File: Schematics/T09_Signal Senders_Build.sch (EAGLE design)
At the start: 35 parts, among them IC1 7805TV, IC2 7805TV, IC3 ATMEGA328, SW1 , X1 , Y2 16MHz

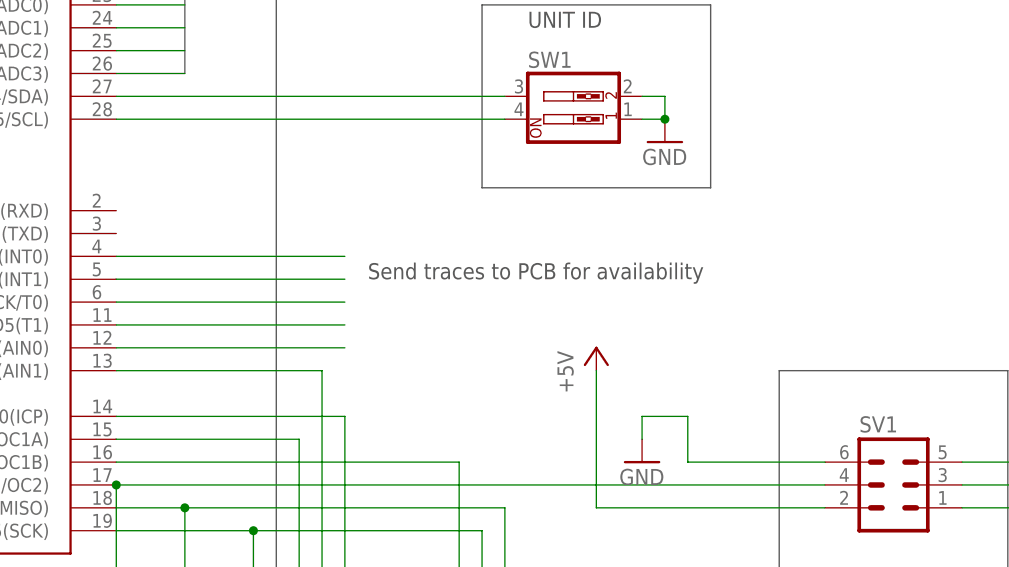
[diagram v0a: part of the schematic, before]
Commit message: PCB - added vias, added headers to uC unused pins
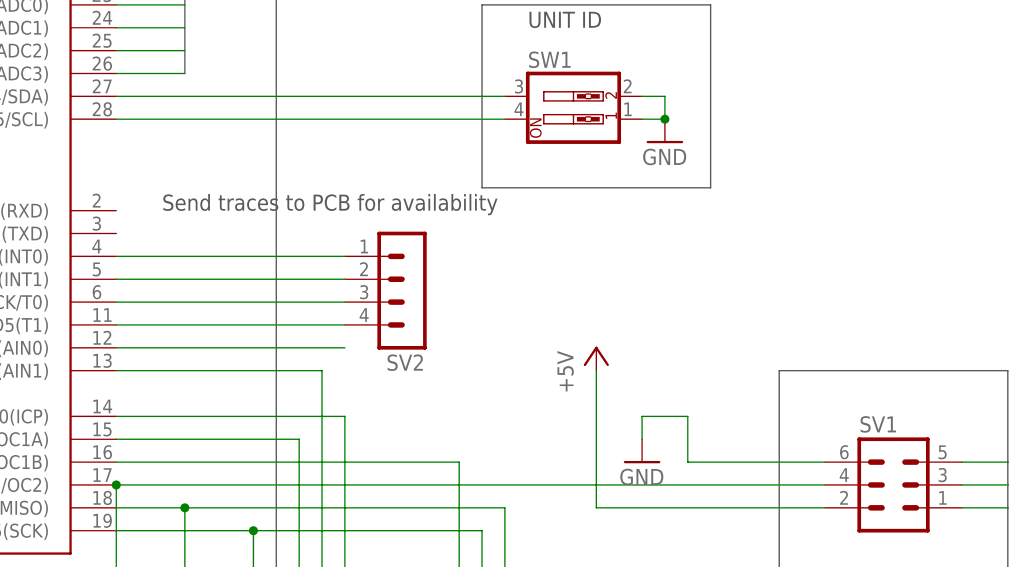
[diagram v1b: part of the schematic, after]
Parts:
- added SV2: (no value), con-lstb:MA04-1
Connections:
- net N$11: now also SV2.1
- net N$12: now also SV2.2
- net N$15: now also SV2.3
- net N$16: now also SV2.4
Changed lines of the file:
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@@
 <layer number="91" name="Nets" color="2" fill="1" visible="yes" active="yes"/>
 <layer number="92" name="Busses" color="1" fill="1" visible="yes" active="yes"/>
-<layer number="93" name="Pins" color="2" fill="1" visible="no" active="yes"/>
+<layer number="93" name="Pins" color="2" fill="1" visible="yes" active="yes"/>
 <layer number="94" name="Symbols" color="4" fill="1" visible="yes" active="yes"/>
 <layer number="95" name="Names" color="7" fill="1" visible="yes" active="yes"/>
 <layer number="96" name="Values" color="7" fill="1" visible="yes" active="yes"/>
 <layer number="97" name="Info" color="7" fill="1" visible="yes" active="yes"/>
-<layer number="98" name="Guide" color="6" fill="1" visible="no" active="yes"/>
+<layer number="98" name="Guide" color="6" fill="1" visible="yes" active="yes"/>
 <layer number="100" name="Muster" color="7" fill="1" visible="no" active="no"/>
-<layer number="101" name="Patch_Top" color="12" fill="4" visible="no" active="yes"/>
-<layer number="102" name="Vscore" color="7" fill="1" visible="no" active="yes"/>
-<layer number="103" name="tMap" color="7" fill="1" visible="no" active="yes"/>
-<layer number="104" name="Name" color="16" fill="1" visible="no" active="yes"/>
-<layer number="105" name="tPlate" color="7" fill="1" visible="no" active="yes"/>
-<layer number="106" name="bPlate" color="7" fill="1" visible="no" active="yes"/>
-<layer number="107" name="Crop" color="7" fill="1" visible="no" active="yes"/>
+<layer number="101" name="Patch_Top" color="12" fill="4" visible="yes" active="yes"/>
+<layer number="102" name="Vscore" color="7" fill="1" visible="yes" active="yes"/>
+<layer number="103" name="tMap" color="7" fill="1" visible="yes" active="yes"/>
+<layer number="104" name="Name" color="16" fill="1" visible="yes" active="yes"/>
+<layer number="105" name="tPlate" color="7" fill="1" visible="yes" active="yes"/>
+<layer number="106" name="bPlate" color="7" fill="1" visible="yes" active="yes"/>
+<layer number="107" name="Crop" color="7" fill="1" visible="yes" active="yes"/>
 <layer number="108" name="tplace-old" color="10" fill="1" visible="yes" active="yes"/>
 <layer number="109" name="ref-old" color="11" fill="1" visible="yes" active="yes"/>
-<layer number="116" name="Patch_BOT" color="9" fill="4" visible="no" active="yes"/>
-<layer number="121" name="_tsilk" color="7" fill="1" visible="no" active="yes"/>
-<layer number="122" name="_bsilk" color="7" fill="1" visible="no" active="yes"/>
-<layer number="125" name="_tNames" color="7" fill="1" visible="no" active="yes"/>
-<layer number="144" name="Drill_legend" color="7" fill="1" visible="no" active="yes"/>
-<layer number="151" name="HeatSink" color="7" fill="1" visible="no" active="yes"/>
+<layer number="116" name="Patch_BOT" color="9" fill="4" visible="yes" active="yes"/>
+<layer number="121" name="_tsilk" color="7" fill="1" visible="yes" active="yes"/>
+<layer number="122" name="_bsilk" color="7" fill="1" visible="yes" active="yes"/>
+<layer number="125" name="_tNames" color="7" fill="1" visible="yes" active="yes"/>
+<layer number="144" name="Drill_legend" color="7" fill="1" visible="yes" active="yes"/>
+<layer number="151" name="HeatSink" color="7" fill="1" visible="yes" active="yes"/>
 <layer number="199" name="Contour" color="7" fill="1" visible="yes" active="yes"/>
-<layer number="200" name="200bmp" color="1" fill="10" visible="no" active="yes"/>
-<layer number="201" name="201bmp" color="2" fill="10" visible="no" active="yes"/>
-<layer number="202" name="202bmp" color="3" fill="10" visible="no" active="yes"/>
-<layer number="203" name="203bmp" color="4" fill="10" visible="no" active="yes"/>
-<layer number="204" name="204bmp" color="5" fill="10" visible="no" active="yes"/>
-<layer number="205" name="205bmp" color="6" fill="10" visible="no" active="yes"/>
-<layer number="206" name="206bmp" color="7" fill="10" visible="no" active="yes"/>
-<layer number="207" name="207bmp" color="8" fill="10" visible="no" active="yes"/>
-<layer number="208" name="208bmp" color="9" fill="10" visible="no" active="yes"/>
-<layer number="209" name="209bmp" color="7" fill="1" visible="no" active="yes"/>
-<layer number="210" name="210bmp" color="7" fill="1" visible="no" active="yes"/>
-<layer number="211" name="211bmp" color="7" fill="1" visible="no" active="yes"/>
-<layer number="212" name="212bmp" color="7" fill="1" visible="no" active="yes"/>
-<layer number="213" name="213bmp" color="7" fill="1" visible="no" active="yes"/>
-<layer number="214" name="214bmp" color="7" fill="1" visible="no" active="yes"/>
-<layer number="215" name="215bmp" color="7" fill="1" visible="no" active="yes"/>
-<layer number="216" name="216bmp" color="7" fill="1" visible="no" active="yes"/>
+<layer number="200" name="200bmp" color="1" fill="10" visible="yes" active="yes"/>
+<layer number="201" name="201bmp" color="2" fill="10" visible="yes" active="yes"/>
+<layer number="202" name="202bmp" color="3" fill="10" visible="yes" active="yes"/>
+<layer number="203" name="203bmp" color="4" fill="10" visible="yes" active="yes"/>
+<layer number="204" name="204bmp" color="5" fill="10" visible="yes" active="yes"/>
+<layer number="205" name="205bmp" color="6" fill="10" visible="yes" active="yes"/>
+<layer number="206" name="206bmp" color="7" fill="10" visible="yes" active="yes"/>
+<layer number="207" name="207bmp" color="8" fill="10" visible="yes" active="yes"/>
+<layer number="208" name="208bmp" color="9" fill="10" visible="yes" active="yes"/>
+<layer number="209" name="209bmp" color="7" fill="1" visible="yes" active="yes"/>
+<layer number="210" name="210bmp" color="7" fill="1" visible="yes" active="yes"/>
+<layer number="211" name="211bmp" color="7" fill="1" visible="yes" active="yes"/>
+<layer number="212" name="212bmp" color="7" fill="1" visible="yes" active="yes"/>
+<layer number="213" name="213bmp" color="7" fill="1" visible="yes" active="yes"/>
+<layer number="214" name="214bmp" color="7" fill="1" visible="yes" active="yes"/>
+<layer number="215" name="215bmp" color="7" fill="1" visible="yes" active="yes"/>
+<layer number="216" name="216bmp" color="7" fill="1" visible="yes" active="yes"/>
 <layer number="217" name="217bmp" color="18" fill="1" visible="no" active="no"/>
 <layer number="218" name="218bmp" color="19" fill="1" visible="no" active="no"/>
@@
 <layer number="250" name="Descript" color="3" fill="1" visible="no" active="no"/>
 <layer number="251" name="SMDround" color="12" fill="11" visible="no" active="no"/>
-<layer number="254" name="cooling" color="7" fill="1" visible="no" active="yes"/>
+<layer number="254" name="cooling" color="7" fill="1" visible="yes" active="yes"/>
 </layers>
 <schematic xreflabel="%F%N/%S.%C%R" xrefpart="/%S.%C%R">
@@
 <part name="P+7" library="supply1" deviceset="+5V" device=""/>
 <part name="GND16" library="supply1" deviceset="GND" device=""/>
+<part name="SV2" library="con-lstb" deviceset="MA04-1" device=""/>
 </parts>
 <sheets>
@@
 <wire x1="147.32" y1="81.28" x2="147.32" y2="182.88" width="0.1524" layer="97"/>
 <wire x1="147.32" y1="182.88" x2="254" y2="182.88" width="0.1524" layer="97"/>
-<text x="264.16" y="119.38" size="1.778" layer="97">Send traces to PCB for availability</text>
+<text x="241.3" y="127" size="1.778" layer="97">Send traces to PCB for availability</text>
 <wire x1="177.8" y1="248.92" x2="177.8" y2="200.66" width="0.1524" layer="97"/>
 <text x="10.16" y="254" size="1.778" layer="97">Connects to a DC barrel on the wall of the unit.
@@
 <instance part="P+7" gate="1" x="289.56" y="111.76"/>
 <instance part="GND16" gate="1" x="294.64" y="99.06"/>
+<instance part="SV2" gate="1" x="269.24" y="116.84" rot="R180"/>
 </instances>
 <busses>
@@
 <pinref part="IC3" gate="G$1" pin="PD2(INT0)"/>
 <wire x1="236.22" y1="121.92" x2="261.62" y2="121.92" width="0.1524" layer="91"/>
+<pinref part="SV2" gate="1" pin="1"/>
 </segment>
 </net>
@@
 <pinref part="IC3" gate="G$1" pin="PD3(INT1)"/>
 <wire x1="236.22" y1="119.38" x2="261.62" y2="119.38" width="0.1524" layer="91"/>
+<pinref part="SV2" gate="1" pin="2"/>
 </segment>
 </net>
@@
 <pinref part="IC3" gate="G$1" pin="PD4(XCK/T0)"/>
 <wire x1="236.22" y1="116.84" x2="261.62" y2="116.84" width="0.1524" layer="91"/>
+<pinref part="SV2" gate="1" pin="3"/>
 </segment>
 </net>
@@
 <pinref part="IC3" gate="G$1" pin="PD5(T1)"/>
 <wire x1="236.22" y1="114.3" x2="261.62" y2="114.3" width="0.1524" layer="91"/>
-</segment>
-</net>
+<pinref part="SV2" gate="1" pin="4"/>
+</segment>
+</net>

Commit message: Fixed Nets. Fixed Silkscreen Layer
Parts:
- 5: value RED -> POWER
- JP1: value (none) -> RF
- JP2: value (none) -> IR
- JP3: value (none) -> Battery; device pinhead:PINHD-1X2/90 -> pinhead:PINHD-1X2
- JP4, JP5, JP6: device pinhead:PINHD-1X2/90 -> pinhead:PINHD-1X2
- LED1: value RED -> WEST
- LED2: value GREEN -> EAST
- LED3: value YELLOW -> SOUTH
- LED4: value BLUE -> NORTH
- S2: value TL32YO -> POWER
- SV1: value (none) -> SPI
- SW1: value (none) -> UNIT_ID
- renumbered LED5 to 5
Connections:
- net RF_SPDSCSC renamed N$35
- net RF_SPI5 renamed N$33
- net RF_SPIDSCSD renamed N$39
- removed net RF_SPIDSCS: IC3.PB4(MISO), JP1.7, JP5.1, JP5.2, SV1.1
- removed net RF_SPIDSCSC: IC3.PB3(MOSI/OC2), JP1.6, JP6.1, JP6.2, SV1.4
- removed net SPI_CE: IC3.PB0(ICP), IC3.PB2(SS/OC1B), JP1.3, JP1.4
- new net N$31: IC3.PB3(MOSI/OC2), IC3.PB4(MISO), JP5.1, JP6.1, SV1.1, SV1.4
- new net N$34: IC3.PB0(ICP), JP1.4
- new net N$36: IC3.PB2(SS/OC1B), JP1.3
- new net N$37: JP1.6, JP6.2
- new net N$38: JP1.7, JP5.2
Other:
- moved on the sheet: C3, JP2, SV1

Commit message: RF nets still had errors. Still need to be routed.
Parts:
- SV2: value (none) -> (none)
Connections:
- new net N$32: IC3.PB3(MOSI/OC2), JP6.1, SV1.4
- net N$31: no longer IC3.PB3(MOSI/OC2), JP6.1, SV1.4
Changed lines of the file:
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@@
 <part name="P+7" library="supply1" deviceset="+5V" device=""/>
 <part name="GND16" library="supply1" deviceset="GND" device=""/>
-<part name="SV2" library="con-lstb" deviceset="MA04-1" device=""/>
+<part name="SV2" library="con-lstb" deviceset="MA04-1" device="" value=" "/>
 </parts>
 <sheets>
@@
 </segment>
 </net>
-<net name="N$31" class="0">
-<segment>
-<pinref part="IC3" gate="G$1" pin="PB3(MOSI/OC2)"/>
-<wire x1="236.22" y1="96.52" x2="304.8" y2="96.52" width="0.1524" layer="91"/>
-<wire x1="304.8" y1="96.52" x2="304.8" y2="104.14" width="0.1524" layer="91"/>
-<pinref part="SV1" gate="1" pin="4"/>
-<wire x1="304.8" y1="104.14" x2="314.96" y2="104.14" width="0.1524" layer="91"/>
-<pinref part="JP6" gate="G$1" pin="1"/>
-<wire x1="236.22" y1="96.52" x2="236.22" y2="93.98" width="0.1524" layer="91"/>
-<pinref part="IC3" gate="G$1" pin="PB4(MISO)"/>
-<wire x1="236.22" y1="93.98" x2="236.22" y2="63.5" width="0.1524" layer="91"/>
-<wire x1="236.22" y1="93.98" x2="243.84" y2="93.98" width="0.1524" layer="91"/>
-<wire x1="243.84" y1="93.98" x2="304.8" y2="93.98" width="0.1524" layer="91"/>
-<wire x1="304.8" y1="93.98" x2="304.8" y2="91.44" width="0.1524" layer="91"/>
-<wire x1="304.8" y1="91.44" x2="340.36" y2="91.44" width="0.1524" layer="91"/>
-<wire x1="340.36" y1="91.44" x2="340.36" y2="101.6" width="0.1524" layer="91"/>
-<pinref part="SV1" gate="1" pin="1"/>
-<wire x1="340.36" y1="101.6" x2="330.2" y2="101.6" width="0.1524" layer="91"/>
-<pinref part="JP5" gate="G$1" pin="1"/>
-<wire x1="243.84" y1="93.98" x2="243.84" y2="63.5" width="0.1524" layer="91"/>
-<junction x="236.22" y="93.98"/>
-<junction x="243.84" y="93.98"/>
-</segment>
-</net>
 <net name="N$33" class="0">
 <segment>
@@
 </segment>
 </net>
+<net name="N$31" class="0">
+<segment>
+<pinref part="IC3" gate="G$1" pin="PB4(MISO)"/>
+<wire x1="236.22" y1="93.98" x2="243.84" y2="93.98" width="0.1524" layer="91"/>
+<wire x1="243.84" y1="93.98" x2="304.8" y2="93.98" width="0.1524" layer="91"/>
+<wire x1="304.8" y1="93.98" x2="304.8" y2="91.44" width="0.1524" layer="91"/>
+<pinref part="SV1" gate="1" pin="1"/>
+<wire x1="340.36" y1="91.44" x2="340.36" y2="101.6" width="0.1524" layer="91"/>
+<wire x1="340.36" y1="101.6" x2="330.2" y2="101.6" width="0.1524" layer="91"/>
+<wire x1="304.8" y1="91.44" x2="340.36" y2="91.44" width="0.1524" layer="91"/>
+<pinref part="JP5" gate="G$1" pin="1"/>
+<wire x1="243.84" y1="63.5" x2="243.84" y2="93.98" width="0.1524" layer="91"/>
+</segment>
+</net>
+<net name="N$32" class="0">
+<segment>
+<pinref part="SV1" gate="1" pin="4"/>
+<wire x1="304.8" y1="104.14" x2="314.96" y2="104.14" width="0.1524" layer="91"/>
+<wire x1="304.8" y1="96.52" x2="304.8" y2="104.14" width="0.1524" layer="91"/>
+<pinref part="IC3" gate="G$1" pin="PB3(MOSI/OC2)"/>
+<wire x1="236.22" y1="96.52" x2="304.8" y2="96.52" width="0.1524" layer="91"/>
+<pinref part="JP6" gate="G$1" pin="1"/>
+<wire x1="236.22" y1="96.52" x2="236.22" y2="63.5" width="0.1524" layer="91"/>
+</segment>
+</net>

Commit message: Minor changes to traces.
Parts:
- S2: device switch:TL32YO -> switch:M251
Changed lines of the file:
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@@
 <part name="D1" library="diode" deviceset="1N4004" device=""/>
 <part name="SW1" library="special" deviceset="SW_DIP-2" device="" value=" UNIT_ID"/>
-<part name="S2" library="switch" deviceset="TL32YO" device="" value="POWER"/>
+<part name="S2" library="switch" deviceset="M251" device="" value="POWER"/>
 <part name="P+5" library="supply1" deviceset="+5V" device=""/>
 <part name="GND12" library="supply1" deviceset="GND" device=""/>
@@
 <instance part="D1" gate="1" x="53.34" y="236.22"/>
 <instance part="SW1" gate="G$1" x="287.02" y="139.7"/>
-<instance part="S2" gate="BEF1" x="63.5" y="236.22" rot="R270"/>
+<instance part="S2" gate="1" x="63.5" y="238.76" rot="R270"/>
 <instance part="P+5" gate="1" x="165.1" y="241.3"/>
 <instance part="GND12" gate="1" x="297.18" y="134.62"/>
@@
 <pinref part="IC1" gate="A1" pin="VI"/>
 <wire x1="68.58" y1="233.68" x2="73.66" y2="233.68" width="0.1524" layer="91"/>
-<pinref part="S2" gate="BEF1" pin="S"/>
+<pinref part="S2" gate="1" pin="S"/>
 <pinref part="C5" gate="G$1" pin="1"/>
 <wire x1="73.66" y1="233.68" x2="83.82" y2="233.68" width="0.1524" layer="91"/>
@@
 <segment>
 <pinref part="D1" gate="1" pin="C"/>
-<pinref part="S2" gate="BEF1" pin="P"/>
+<pinref part="S2" gate="1" pin="P"/>
 <wire x1="55.88" y1="236.22" x2="58.42" y2="236.22" width="0.1524" layer="91"/>
 <wire x1="58.42" y1="236.22" x2="60.96" y2="236.22" width="0.1524" layer="91"/>

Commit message: Andrew's fixes from office hours
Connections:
- removed net N$17: IC3.PD6(AIN0)
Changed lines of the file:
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@@
 <layer number="91" name="Nets" color="2" fill="1" visible="yes" active="yes"/>
 <layer number="92" name="Busses" color="1" fill="1" visible="yes" active="yes"/>
-<layer number="93" name="Pins" color="2" fill="1" visible="yes" active="yes"/>
+<layer number="93" name="Pins" color="2" fill="1" visible="no" active="yes"/>
 <layer number="94" name="Symbols" color="4" fill="1" visible="yes" active="yes"/>
 <layer number="95" name="Names" color="7" fill="1" visible="yes" active="yes"/>
@@
 </segment>
 </net>
-<net name="N$17" class="0">
-<segment>
-<pinref part="IC3" gate="G$1" pin="PD6(AIN0)"/>
-<wire x1="236.22" y1="111.76" x2="261.62" y2="111.76" width="0.1524" layer="91"/>
-</segment>
-</net>
 <net name="+3V3" class="0">
 <segment>
@@
 <pinref part="JP5" gate="G$1" pin="1"/>
 <wire x1="243.84" y1="63.5" x2="243.84" y2="93.98" width="0.1524" layer="91"/>
+<junction x="243.84" y="93.98"/>
 </segment>
 </net>
@@
 <wire x1="304.8" y1="96.52" x2="304.8" y2="104.14" width="0.1524" layer="91"/>
 <pinref part="IC3" gate="G$1" pin="PB3(MOSI/OC2)"/>
-<wire x1="236.22" y1="96.52" x2="304.8" y2="96.52" width="0.1524" layer="91"/>
+<wire x1="236.22" y1="96.52" x2="238.76" y2="96.52" width="0.1524" layer="91"/>
 <pinref part="JP6" gate="G$1" pin="1"/>
-<wire x1="236.22" y1="96.52" x2="236.22" y2="63.5" width="0.1524" layer="91"/>
-</segment>
-</net>
+<wire x1="238.76" y1="96.52" x2="304.8" y2="96.52" width="0.1524" layer="91"/>
+<wire x1="236.22" y1="86.36" x2="236.22" y2="63.5" width="0.1524" layer="91"/>
+<wire x1="236.22" y1="86.36" x2="238.76" y2="86.36" width="0.1524" layer="91"/>
+<wire x1="238.76" y1="86.36" x2="238.76" y2="96.52" width="0.1524" layer="91"/>
+<junction x="238.76" y="96.52"/>
+</segment>
+</net>

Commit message: Fixes as per Andrews recommendations
vcc lines larger, gnd vias, move crystal and bypass caps, add diode to
battery, version, names
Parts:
- added D2: 1N4004, diode:1N4004
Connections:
- new net N$13: D2.A, JP3.1
- net +9V: now also D2.C; no longer JP3.1
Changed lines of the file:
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@@
 <part name="GND16" library="supply1" deviceset="GND" device=""/>
 <part name="SV2" library="con-lstb" deviceset="MA04-1" device="" value=" "/>
+<part name="D2" library="diode" deviceset="1N4004" device=""/>
 </parts>
 <sheets>
@@
 <instance part="GND16" gate="1" x="294.64" y="106.68"/>
 <instance part="SV2" gate="1" x="269.24" y="116.84" rot="R180"/>
+<instance part="D2" gate="1" x="48.26" y="223.52" rot="R90"/>
 </instances>
 <busses>
@@
 <pinref part="X1" gate="G$1" pin="1"/>
 <wire x1="40.64" y1="236.22" x2="48.26" y2="236.22" width="0.1524" layer="91"/>
-<pinref part="JP3" gate="G$1" pin="1"/>
+<pinref part="D2" gate="1" pin="C"/>
 <wire x1="48.26" y1="236.22" x2="50.8" y2="236.22" width="0.1524" layer="91"/>
-<wire x1="48.26" y1="210.82" x2="48.26" y2="236.22" width="0.1524" layer="91"/>
+<wire x1="48.26" y1="226.06" x2="48.26" y2="236.22" width="0.1524" layer="91"/>
 <junction x="48.26" y="236.22"/>
 </segment>
@@
 </segment>
 </net>
+<net name="N$13" class="0">
+<segment>
+<pinref part="D2" gate="1" pin="A"/>
+<pinref part="JP3" gate="G$1" pin="1"/>
+<wire x1="48.26" y1="220.98" x2="48.26" y2="210.82" width="0.1524" layer="91"/>
+</segment>
+</net>
 </nets>
 </sheet>
 </sheets>
-<errors>
-</errors>
 </schematic>
 </drawing>
